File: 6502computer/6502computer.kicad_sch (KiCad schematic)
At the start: 28 parts

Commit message: Update schematics
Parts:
- removed U? (x3): 74AHC1G32, symbol 74xGxx:74AHC1G32
- removed U? (x5): 74AHCT04, symbol 74xx:74AHCT04
- removed U?: 74LS00, symbol 74xx:74LS00
- removed X?: SG-5032CAN, Oscillator:Oscillator_SMD_SeikoEpson_SG8002LB-4Pin_5.0x3.2mm, symbol Oscillator:SG-5032CAN
- added C1, C2, C3, C4, C6, C7, C9: 1 uF, symbol Device:C_Small
- added J1: DB9_Male, symbol Connector:DB9_Male
- added U10: 74LS32, symbol 74xx:74LS32
- added U6: MAX233CPP+G36, 21-0043D_20_MXM, symbol max233:MAX233CPP+G36
- added U8: 74HCT04, symbol 74xx:74HCT04
- added U9: 74HC00, symbol 74xx:74HC00
- added Y1: ECS-2100AX-1.0MHZ, ECS2100AX10MHZ, symbol SamacSys_Parts:ECS-2100AX-1.0MHZ
- C5, C8: renamed from C?; value C_Small -> 1 uF
- R1: renamed from R?; value R -> 1 kOhm
- RV1: renamed from RV?; value R_Potentiometer_Trim_US -> 10 kOhm
- gave numbers to parts that had none: 11
- renumbered C to C10, R to R2, R to R3
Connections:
- net 1 MHz Clock is gone; now on net CLK: U3.27 (ϕ2)
- net +5V: now also C8.2, C1.1, C2.1, C3.1, C4.1, C6.1, C7.1, C9.1, U6.7 (VCC), Y1.8 (+5V_DC); no longer C8.1
- net GNDREF: now also C8.1, RESET.1 (A), RESET.2 (A), C1.2, C2.2, C3.2, C4.2, C6.2, C7.2, C9.2, J1.5, U6.6 (GND), U6.9 (GND), Y1.4 (GROUND); no longer C8.2, RESET.3 (B), RESET.4 (B), U3.3 (~{CS2}), U7.10 (Y5)
- net VIA CS2B: no longer U2.35 (RS3), U2.36 (RS2), U2.37 (RS1), U2.38 (RS0), U3.13 (RS0), U3.14 (RS1)
- net y0b: now also U10.5, U8.6
- net y1b: now also U10.2, U8.4
- net y2b: now also U10.1, U8.2
- net y3b: now also U10.10, U8.8
- net at U7.12 (Y3): now also U8.9; no longer U7.15 (Y0)
- net at R1.2, U1.40 (~{RES}), U2.34 (~{RES})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: now also RESET.3 (B), RESET.4 (B); no longer RESET.1 (A), RESET.2 (A)
- net CLK: now reaches U2.25 (ϕ2)
- net CLK: now also U1.37 (ϕ0), U9.1, Y1.5 (OUTPUT)
- net at U5.20 (~{CS}): now also U9.3
- net at U5.22 (~{OE}): now also U8.10
- net at U7.13 (Y2): now also U8.1
- net at U7.14 (Y1): now also U8.3
- net T1IN: now reaches U3.10 (TxD)
- net R1OUT: now reaches U3.12 (RxD)
- net ACIA CS2B: now reaches U3.18 (D0)
- net ACIA CS2B: now also U3.19 (D1), U3.20 (D2), U3.21 (D3), U3.22 (D4), U3.23 (D5), U3.24 (D6), U3.25 (D7), U3.3 (~{CS2}), U7.10 (Y5)
- new net: U6.10 (CS-), U6.16 (C2-)
- new net: U6.11 (C2+), U6.15 (C2+)
- new net: U6.12 (V-), U6.17 (V-)
- new net: U10.8, U8.11, U9.2
- new net: U10.6, U10.9
- new net: U7.15 (Y0), U8.5
- new net: U10.3, U10.4
- new net RxD (To DTE TxD): J1.2, U6.4 (R1IN)
- new net TxD (To DTE RxD): J1.3, U6.5 (T1OUT)
- new net UART RxD: U6.3 (R1OUT)
- new net UART TxD: U6.2 (T1IN)
- new net a0: U2.38 (RS0), U3.13 (RS0)
- new net a1: U2.37 (RS1), U3.14 (RS1)
- new net a2: U2.36 (RS2)
- new net a3: U2.35 (RS3)
- no-connect marks 11 -> 15
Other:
- note added: "(MAX233 connected to DTE without separate null modem)"
- note added: "65C02 BEATER"
- note added: "Address Space: 0000-7FFF RAM 8000-9FFF VIA A000-BFFF ACIA C000-DFFF unassigned E000-FFFF ROM"
- moved on the sheet: C10, C5, C8, D1, LCD, R2, R3, RESET, RV1, RV2, U1, U2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

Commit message: Remove backups Change Tx delay routine
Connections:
- net at R3.2, U3.7 (XTAL2), Y2.1: no longer C10.2
- net at R3.1, U3.6 (XTAL1), Y2.2: now also C10.2
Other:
- moved on the sheet: C10
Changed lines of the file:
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@@
   (junction (at 25.4 19.05) (diameter 0) (color 0 0 0 0)
   )
-  (junction (at 220.98 38.1) (diameter 0) (color 0 0 0 0)
-  )
   (junction (at 168.91 114.3) (diameter 0) (color 0 0 0 0)
   )
@@
   )
   (junction (at 143.51 16.51) (diameter 0) (color 0 0 0 0)
+  )
+  (junction (at 220.98 30.48) (diameter 0) (color 0 0 0 0)
   )
   (no_connect (at 78.74 58.42))
@@
     (stroke (width 0) (type default) (color 0 0 0 0))
   )
-  (wire (pts (xy 213.36 38.1) (xy 220.98 38.1))
+  (wire (pts (xy 213.36 38.1) (xy 229.87 38.1))
     (stroke (width 0) (type default) (color 0 0 0 0))
   )
@@
     (stroke (width 0) (type default) (color 0 0 0 0))
   )
+  (wire (pts (xy 220.98 30.48) (xy 220.98 21.59))
+    (stroke (width 0) (type default) (color 0 0 0 0))
+  )
   (bus (pts (xy 123.19 93.98) (xy 123.19 110.49))
     (stroke (width 0) (type default) (color 0 0 0 0))
@@
     (stroke (width 0) (type default) (color 0 0 0 0))
   )
+  (wire (pts (xy 220.98 30.48) (xy 229.87 30.48))
+    (stroke (width 0) (type default) (color 0 0 0 0))
+  )
   (wire (pts (xy 231.14 81.28) (xy 231.14 99.06))
     (stroke (width 0) (type default) (color 0 0 0 0))
@@
     (stroke (width 0) (type default) (color 0 0 0 0))
   )
-  (wire (pts (xy 220.98 38.1) (xy 229.87 38.1))
-    (stroke (width 0) (type default) (color 0 0 0 0))
-  )
   (bus (pts (xy 109.22 132.08) (xy 109.22 134.62))
     (stroke (width 0) (type default) (color 0 0 0 0))
@@
     (stroke (width 0) (type default) (color 0 0 0 0))
   )
+  (wire (pts (xy 226.06 24.13) (xy 226.06 21.59))
+    (stroke (width 0) (type default) (color 0 0 0 0))
+  )
   (wire (pts (xy 55.88 156.21) (xy 64.77 156.21))
     (stroke (width 0) (type default) (color 0 0 0 0))
@@
     (stroke (width 0) (type default) (color 0 0 0 0))
   )
-  (wire (pts (xy 213.36 30.48) (xy 229.87 30.48))
+  (wire (pts (xy 213.36 30.48) (xy 220.98 30.48))
     (stroke (width 0) (type default) (color 0 0 0 0))
   )
@@
   )
   (wire (pts (xy 173.99 102.87) (xy 173.99 91.44))
-    (stroke (width 0) (type default) (color 0 0 0 0))
-  )
-  (wire (pts (xy 220.98 39.37) (xy 220.98 38.1))
     (stroke (width 0) (type default) (color 0 0 0 0))
   )
@@
     (pin "4")
   )
-  (symbol (lib_id "power:GNDREF") (at 220.98 44.45 0) (unit 1)
+  (symbol (lib_id "power:GNDREF") (at 226.06 24.13 0) (unit 1)
     (in_bom yes) (on_board yes) (fields_autoplaced)
-    (property "Reference" "#PWR?" (id 0) (at 220.98 50.8 0)
+    (property "Reference" "#PWR?" (id 0) (at 226.06 30.48 0)
       (effects (font (size 1.27 1.27)) hide)
     )
-    (property "Value" "GNDREF" (id 1) (at 220.98 49.53 0))
-    (property "Footprint" "" (id 2) (at 220.98 44.45 0)
+    (property "Value" "GNDREF" (id 1) (at 226.06 29.21 0))
+    (property "Footprint" "" (id 2) (at 226.06 24.13 0)
       (effects (font (size 1.27 1.27)) hide)
     )
-    (property "Datasheet" "" (id 3) (at 220.98 44.45 0)
+    (property "Datasheet" "" (id 3) (at 226.06 24.13 0)
       (effects (font (size 1.27 1.27)) hide)
     )
     (pin "1")
   )
-  (symbol (lib_id "Device:C_Small") (at 220.98 41.91 180) (unit 1)
+  (symbol (lib_id "Device:C_Small") (at 223.52 21.59 270) (unit 1)
     (in_bom yes) (on_board yes) (fields_autoplaced)
-    (property "Reference" "C10" (id 0) (at 223.52 40.6335 0)
-      (effects (font (size 1.27 1.27)) (justify right))
-    )
-    (property "Value" "30 pF" (id 1) (at 223.52 43.1735 0)
-      (effects (font (size 1.27 1.27)) (justify right))
-    )
-    (property "Footprint" "" (id 2) (at 220.98 41.91 0)
+    (property "Reference" "C10" (id 0) (at 223.5136 15.24 90))
+    (property "Value" "30 pF" (id 1) (at 223.5136 17.78 90))
+    (property "Footprint" "" (id 2) (at 223.52 21.59 0)
       (effects (font (size 1.27 1.27)) hide)
     )
-    (property "Datasheet" "~" (id 3) (at 220.98 41.91 0)
+    (property "Datasheet" "~" (id 3) (at 223.52 21.59 0)
       (effects (font (size 1.27 1.27)) hide)
     )

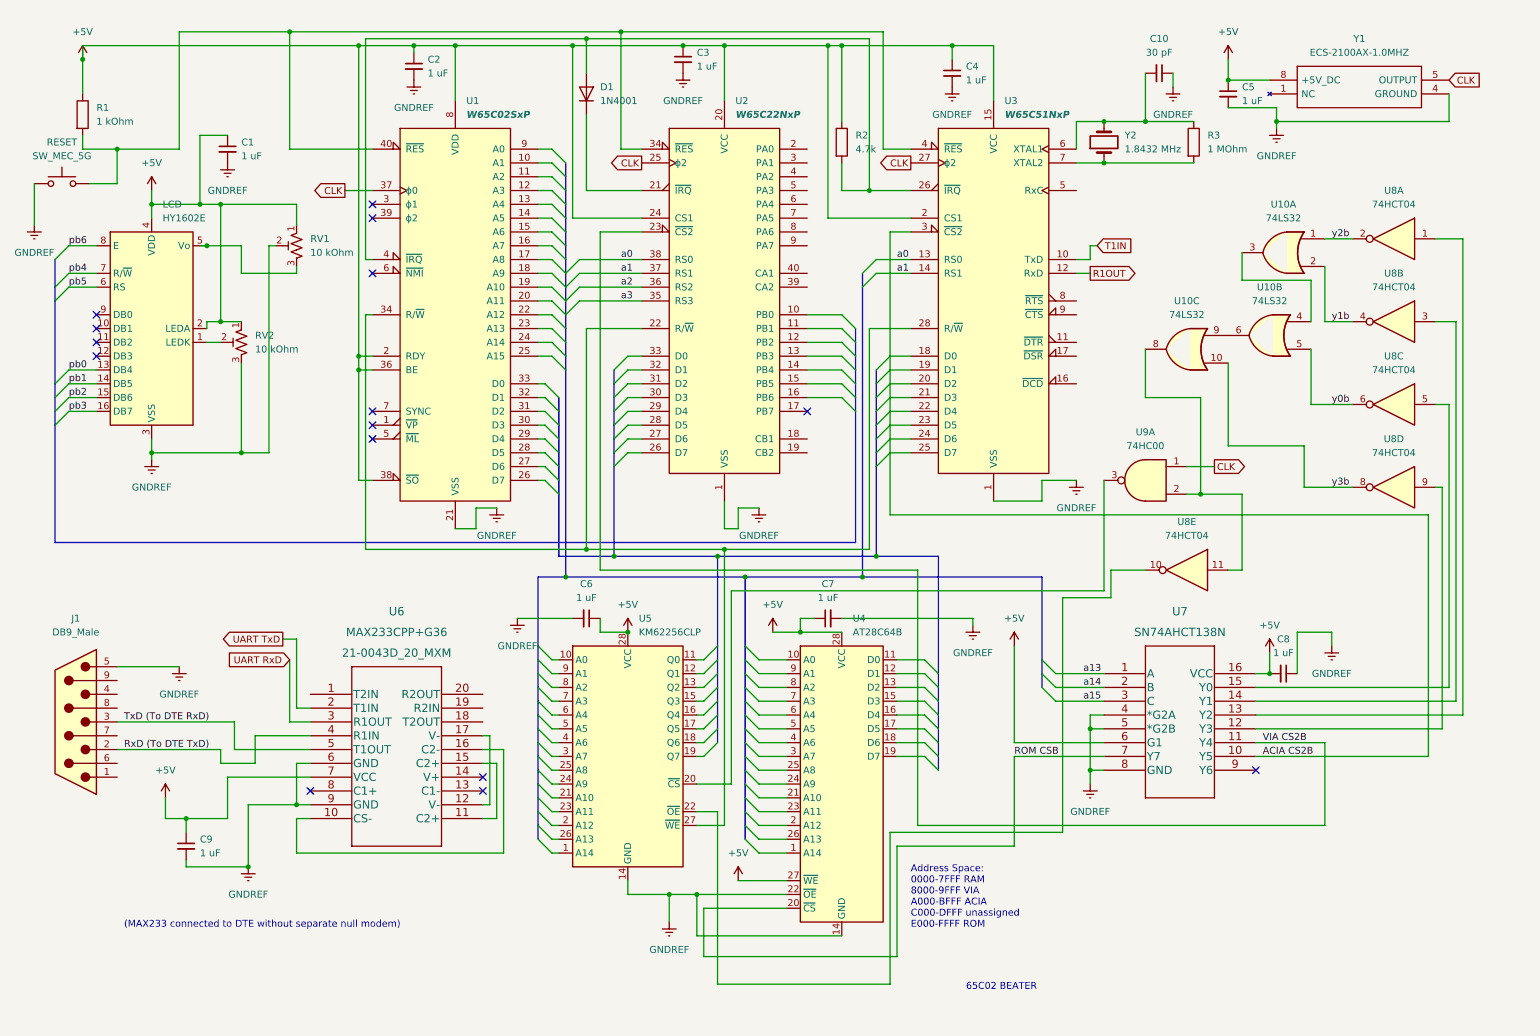
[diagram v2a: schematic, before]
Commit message: Reorganize schematic
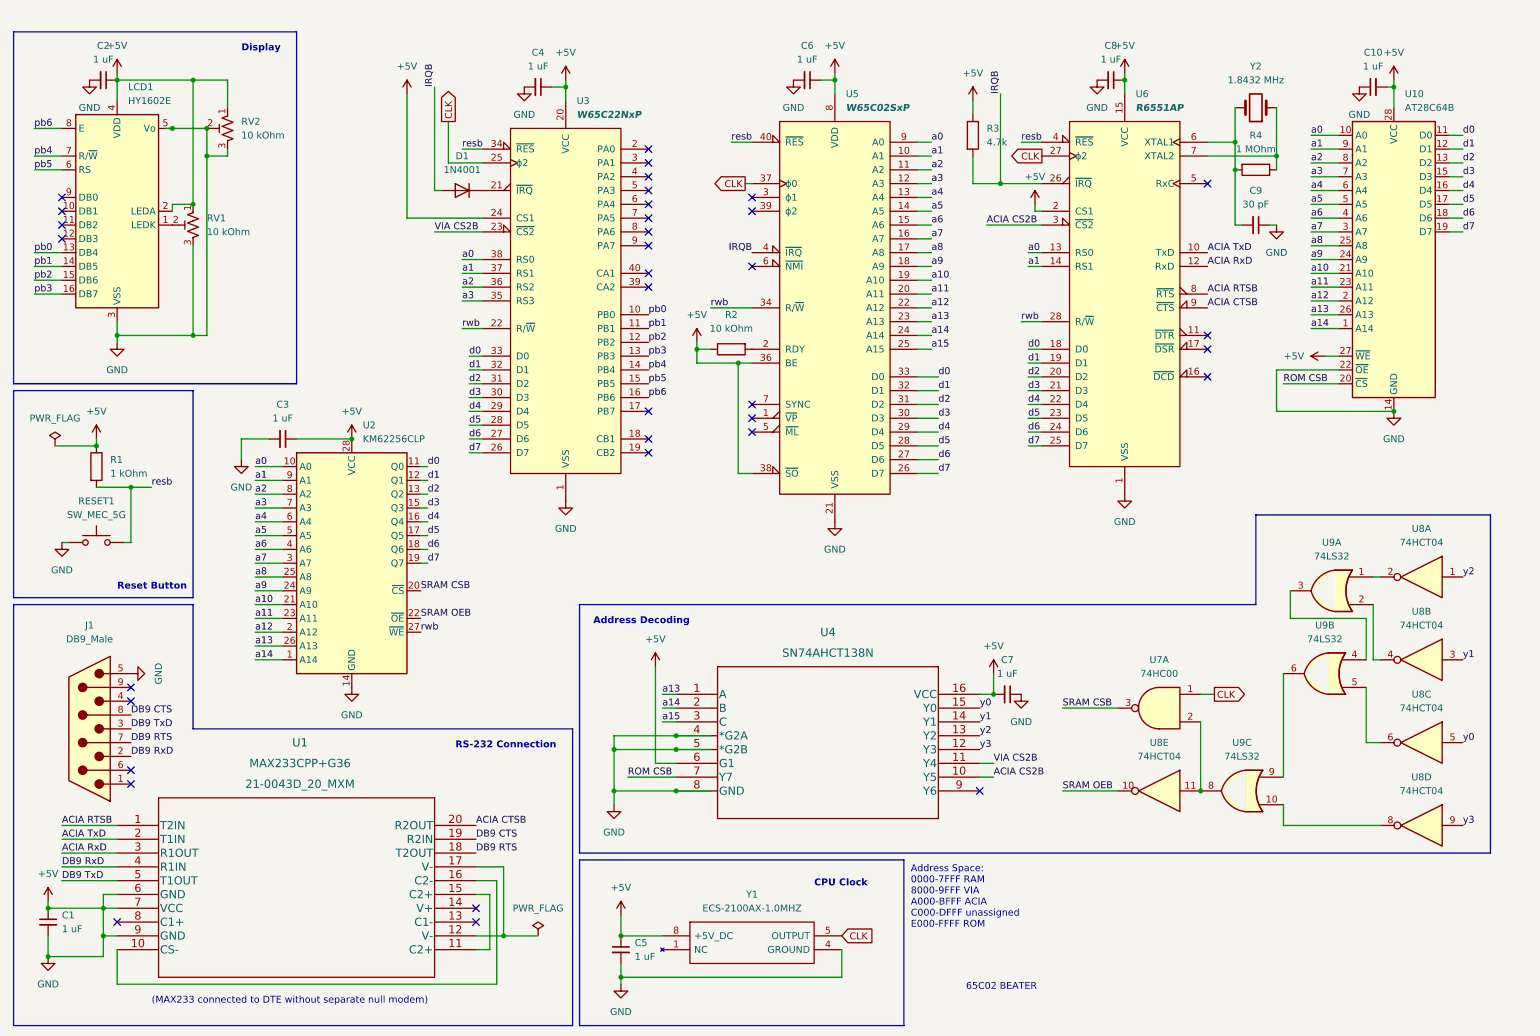
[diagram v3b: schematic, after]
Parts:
- removed C1, C3: 1 uF, symbol Device:C_Small
- removed C10: 30 pF, symbol Device:C_Small
- added C6, C8: 1 uF, symbol Device:C_Small
- added C9: 30 pF, symbol Device:C_Small
- added R2: 10 kOhm, symbol Device:R
- U6: renamed from U3; value W65C51NxP -> R6551AP
- renumbered C9 to C1, C7 to C10, C6 to C3, C8 to C7, LCD to LCD1, R2 to R3, R3 to R4, RESET to RESET1, RV2 to RV1, RV1 to RV2, U6 to U1, U4 to U10, U5 to U2, U2 to U3, U7 to U4, U1 to U5, U9 to U7, U10 to U9
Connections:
- net GNDREF is gone; now on net +5V: C1.2, C10.2, C2.2, C3.2, C4.2, C5.2, C7.1, J1.5, LCD1.3 (VSS), RESET1.1 (A), RESET1.2 (A), RV1.3, RV2.2, U1.6 (GND), U1.9 (GND), U10.14 (GND), U10.22 (~{OE}), U2.14 (GND), U3.1 (VSS), U4.4 (*G2A), U4.5 (*G2B), U4.8 (GND), U5.21 (VSS), U6.1 (VSS), Y1.4 (GROUND)
- net UART RxD is gone; now on net ACIA RxD: U1.3 (R1OUT)
- net UART TxD is gone; now on net ACIA TxD: U1.2 (T1IN)
- net +5V: now also LCD1.5 (Vo), RV2.3, C6.1, C6.2, C8.1, C8.2, C9.1, R2.1; no longer U5.2 (RDY)
- net ACIA CS2B: no longer U6.18 (D0), U6.19 (D1), U6.20 (D2), U6.21 (D3), U6.22 (D4), U6.23 (D5), U6.24 (D6), U6.25 (D7)
- net a0: now also U10.10 (A0), U2.10 (A0), U5.9 (A0)
- net a1: now also U10.9 (A1), U2.9 (A1), U5.10 (A1)
- net a13: now also U10.26 (A13), U2.26 (A13), U5.23 (A13)
- net a14: now also U10.1 (A14), U2.1 (A14), U5.24 (A14)
- net a15: now also U5.25 (A15)
- net a2: now also U10.8 (A2), U2.8 (A2), U5.11 (A2)
- net a3: now also U10.7 (A3), U2.7 (A3), U5.12 (A3)
- net pb0: now also U3.10 (PB0)
- net pb1: now also U3.11 (PB1)
- net pb2: now also U3.12 (PB2)
- net pb3: now also U3.13 (PB3)
- net pb4: now also U3.14 (PB4)
- net pb5: now also U3.15 (PB5)
- net pb6: now also U3.16 (PB6)
- net ACIA RTSB: now reaches U1.1 (T2IN)
- net ACIA RTSB: now also U6.8 (~{RTS})
- net DB9 RTS: now reaches U1.18 (T2OUT)
- net DB9 RTS: now also J1.7
- net DB9 CTS: now reaches U1.19 (R2IN)
- net DB9 CTS: now also J1.8
- net ACIA CTSB: now reaches U1.20 (R2OUT)
- net ACIA CTSB: now also U6.9 (~{CTS})
- net resb: now reaches R1.2, RESET1.3 (B), RESET1.4 (B), U3.34 (~{RES}), U5.40 (~{RES}), U6.4 (~{RES})
- net at U6.6 (XTAL1), Y2.2: now also R4.2, C9.2; no longer R4.1
- net rwb: now reaches U2.27 (~{WE}), U3.22 (R/~{W}), U5.34 (R/~{W}), U6.28 (R/~{W})
- net d7: now reaches U3.26 (D7)
- net d7: now also U10.19 (D7), U2.19 (Q7), U5.26 (D7), U6.25 (D7)
- net d6: now reaches U3.27 (D6)
- net d6: now also U10.18 (D6), U2.18 (Q6), U5.27 (D6), U6.24 (D6)
- net d5: now reaches U3.28 (D5)
- net d5: now also U10.17 (D5), U2.17 (Q5), U5.28 (D5), U6.23 (D5)
- net d4: now reaches U3.29 (D4)
- net d4: now also U10.16 (D4), U2.16 (Q4), U5.29 (D4), U6.22 (D4)
- net d3: now reaches U3.30 (D3)
- net d3: now also U10.15 (D3), U2.15 (Q3), U5.30 (D3), U6.21 (D3)
- net d2: now reaches U3.31 (D2)
- net d2: now also U10.13 (D2), U2.13 (Q2), U5.31 (D2), U6.20 (D2)
- net d1: now reaches U3.32 (D1)
- net d1: now also U10.12 (D1), U2.12 (Q1), U5.32 (D1), U6.19 (D1)
- net d0: now reaches U3.33 (D0)
- net d0: now also U10.11 (D0), U2.11 (Q0), U5.33 (D0), U6.18 (D0)
- net y1: now reaches U4.14 (Y1), U8.3
- net a4: now reaches U5.13 (A4)
- net a4: now also U10.6 (A4), U2.6 (A4)
- net a5: now reaches U5.14 (A5)
- net a5: now also U10.5 (A5), U2.5 (A5)
- net a6: now reaches U5.15 (A6)
- net a6: now also U10.4 (A6), U2.4 (A6)
- net a7: now reaches U5.16 (A7)
- net a7: now also U10.3 (A7), U2.3 (A7)
- net a8: now reaches U5.17 (A8)
- net a8: now also U10.25 (A8), U2.25 (A8)
- net a9: now reaches U5.18 (A9)
- net a9: now also U10.24 (A9), U2.24 (A9)
- net a10: now reaches U5.19 (A10)
- net a10: now also U10.21 (A10), U2.21 (A10)
- net a11: now reaches U5.20 (A11)
- net a11: now also U10.23 (A11), U2.23 (A11)
- net a12: now reaches U5.22 (A12)
- net a12: now also U10.2 (A12), U2.2 (A12)
- net IRQB: now reaches D1.2 (A), R3.2, U5.4 (~{IRQ}), U6.26 (~{IRQ})
- net y3: now reaches U4.12 (Y3), U8.9
- net SRAM CSB: now reaches U2.20 (~{CS}), U7.3
- net SRAM OEB: now reaches U2.22 (~{OE}), U8.10
- net y2: now reaches U4.13 (Y2), U8.1
- net y0: now reaches U4.15 (Y0), U8.5
- net at U6.7 (XTAL2), Y2.1: now also R4.1; no longer R4.2
- net R1OUT renamed ACIA RxD
- net RxD (To DTE TxD) renamed DB9 RxD
- net T1IN renamed ACIA TxD
- net TxD (To DTE RxD) renamed DB9 TxD
- net y0b: no longer names the net of U8.6, U9.5
- net y1b: no longer names the net of U8.4, U9.2
- net y2b: no longer names the net of U8.2, U9.1
- net y3b: no longer names the net of U8.8, U9.10
- new net: R2.2, U5.2 (RDY)
- no-connect marks 15 -> 35
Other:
- note added: "Address Decoding"
- note added: "CPU Clock"
- note added: "Display"
- note added: "RS-232 Connection"
- note added: "Reset Button"
- moved on the sheet: C1, C10, C3, C5, C7, J1, LCD1, R1, R3, R4, RESET1, RV1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
